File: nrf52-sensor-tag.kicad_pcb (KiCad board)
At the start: 2 copper layers, 36 x 33 mm, 22 parts, among them IC2 VEML6030, IC3 MS860702BA01-50, J3 Conn_01x07_Male, SW1 EVQ-PUA02K, SW2 EVQ-PUA02K, U1 MS88SF2

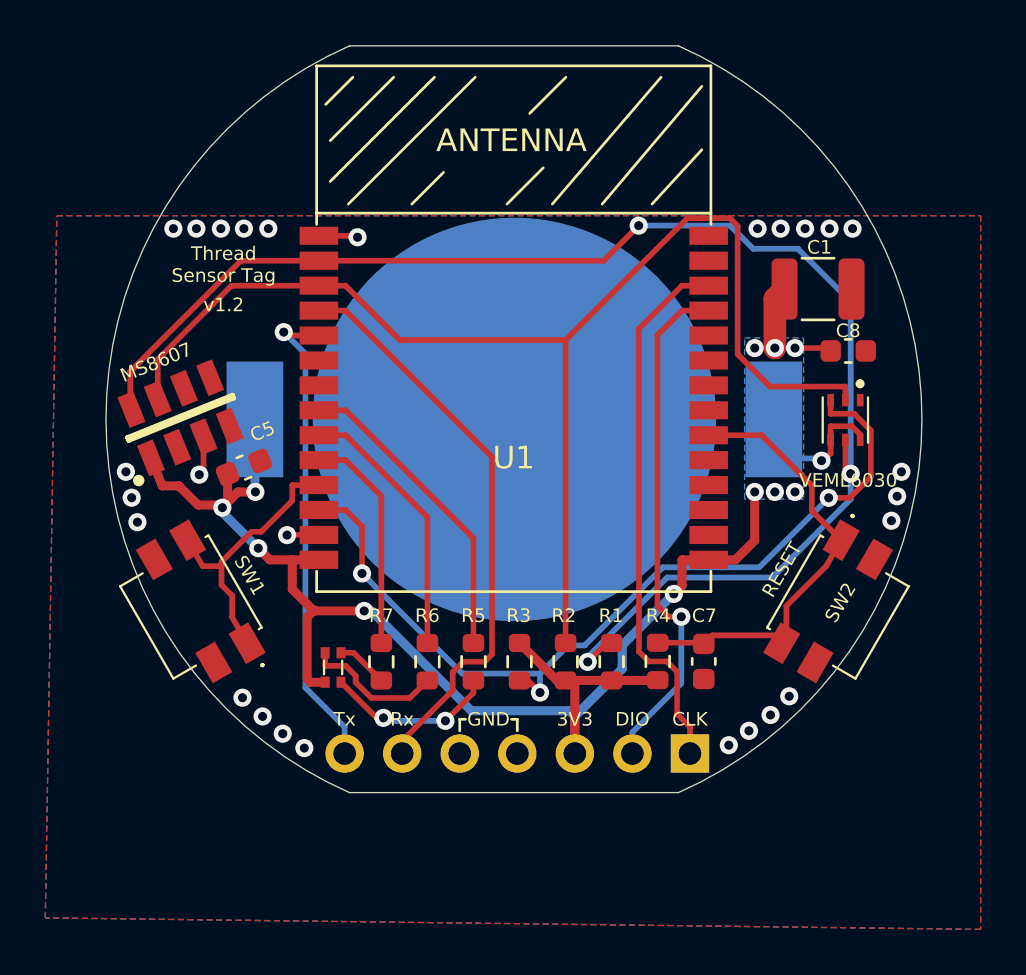
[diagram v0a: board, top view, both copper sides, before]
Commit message: Replaced light sensor VEML6030 with LTR-308ALS-01
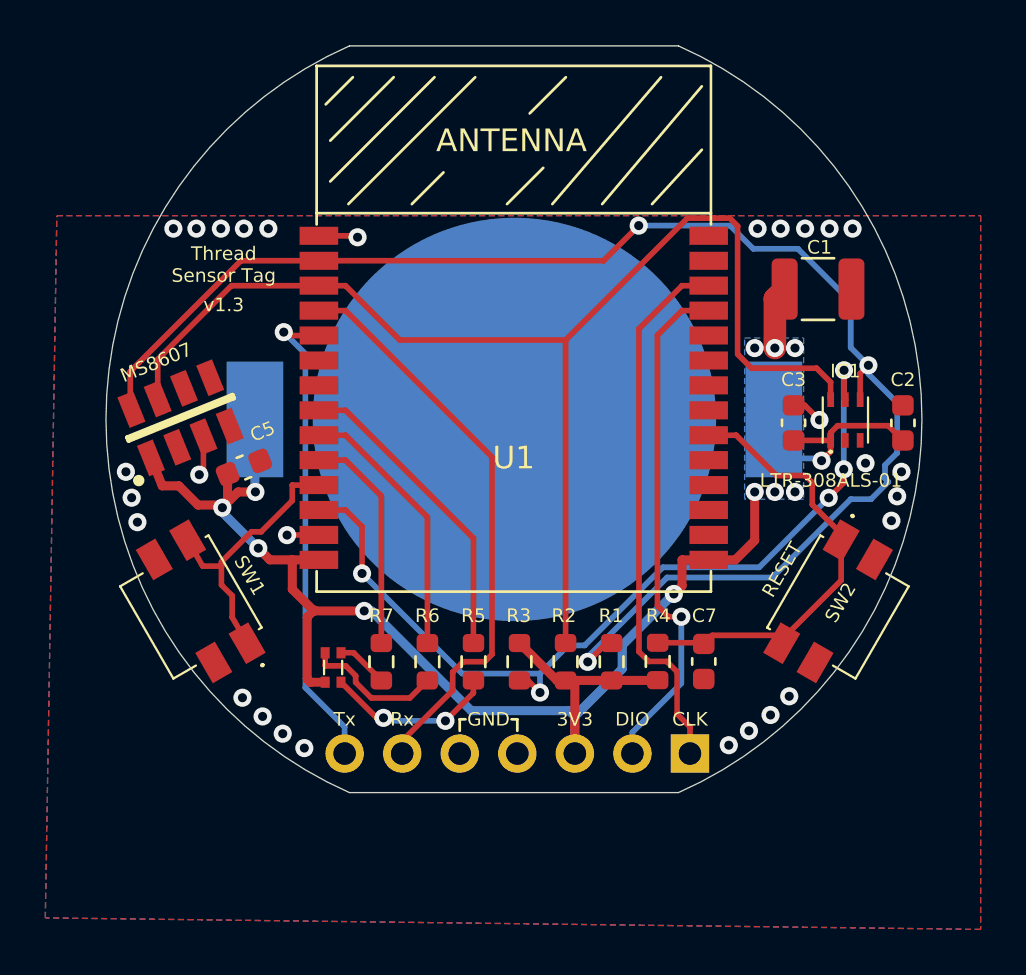
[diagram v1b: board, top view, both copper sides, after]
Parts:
- removed C8: 0.1uF, Capacitor_SMD:C_0603_1608Metric
- removed IC2: VEML6030, VEML6030:VEML6030
- added C2: 4.7uF, Capacitor_SMD:C_0603_1608Metric, F.Cu at (138.9, 64.8)
- added C3: 0.1uF, Capacitor_SMD:C_0603_1608Metric, F.Cu at (134.1, 64.8)
- added IC1: LTR-308ALS-01, LTR-308ALS-01:LTR303ALS01, F.Cu at (136.4, 64.6)
- R3: value 10k -> 4.7k
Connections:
- IC3 pad 2: Net-(IC3-Pad2) -> unconnected-(IC3-Pad2)
- IC3 pad 4: Net-(IC3-Pad4) -> unconnected-(IC3-Pad4)
- IC3 pad 5: Net-(IC3-Pad5) -> unconnected-(IC3-Pad5)
- IC3 pad 6: Net-(IC3-Pad6) -> unconnected-(IC3-Pad6)
- U1 pad 19: Net-(U1-Pad19) -> unconnected-(U1-Pad19)
- U1 pad 20: Net-(U1-Pad20) -> unconnected-(U1-Pad20)
- U1 pad 21: Net-(U1-Pad21) -> unconnected-(U1-Pad21)
- U1 pad 22: Net-(U1-Pad22) -> unconnected-(U1-Pad22)
- U1 pad 24: Net-(U1-Pad24) -> unconnected-(U1-Pad24)
- U1 pad 25: Net-(U1-Pad25) -> unconnected-(U1-Pad25)
- U1 pad 6: Net-(U1-Pad6) -> unconnected-(U1-Pad6)
- U1 pad 7: Net-(U1-Pad7) -> unconnected-(U1-Pad7)
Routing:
- net /SCL: track 64.0 -> 66.4 mm
- net /VCC: track 72.6 -> 74.2 mm
- net GND: track 4.90 -> 6.31 mm, vias 27 -> 29
- net /SDA: track 57.1 -> 56.5 mm
- net /INT1: track 38.8 -> 39.1 mm, vias 3 -> 5
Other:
- net class Default removed
- net class Power removed
- board text added: "LTR-308ALS-01"
- board text added: "v1.3"
- board text removed: "VEML6030"
- board text removed: "v1.2"
